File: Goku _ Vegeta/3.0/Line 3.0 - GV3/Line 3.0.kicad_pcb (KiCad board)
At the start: 2 copper layers, 206 x 197.4 mm, 111 parts, among them J1 BATTERY POWER, J10 Motor 4, J11 LEFT HEADERS, J12 RIGHT HEADERS, J13 MID HEADERS, J2 BACKUP 5V, J3 BACKUP 3V3, J4 I2C, J5 Kicker Voltmeter, J6 Solenoid, J7 Motor 1, J8 Motor 2, J9 Motor 3, Q1 BSC040N10NS5, U1 TPS62132, U2 TPS62133, U3 LM2587S-ADJ, U4 TB67H420FTG Dual/Single Motor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, U5 TB67H420FTG Dual/Single Motor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, U6 TB67H420FTG Dual/Single Motor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, U7 TB67H420FTG Dual/Single Motor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, U8 DEV-16771

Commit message: LINE PCB 3.0 BASICALLY DONE!! NOW JUST GOTTA ADD SILKSCREEN!
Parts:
- removed C1, C2: 10uF, Capacitor_SMD:C_0805_2012Metric
- removed C3, C4: 0.1uF, Capacitor_SMD:C_0805_2012Metric
- removed C5, C6: 3.3nF, Capacitor_SMD:C_0805_2012Metric
- removed C7, C8: 22uF, Capacitor_SMD:C_0805_2012Metric
- removed D1, D2: STTH2002G-TR, Package_TO_SOT_SMD:TO-263-2
- removed J5: Kicker Voltmeter, TerminalBlock:TerminalBlock_bornier-2_P5.08mm
- removed L1, L2: 2.2uH, Inductor_SMD:L_Bourns_SRR1260
- removed R33, R34: 100K, Resistor_SMD:R_0805_2012Metric
- added C14: 100uF, Capacitor_THT:CP_Radial_D10.0mm_P5.00mm, F.Cu at (116.8, 87.5)
- added LED17: JB2835AWT-W-U30GA0000-N0000001, JB2835AWT-W-U30GA0000-N0000001:LED_J2835_CRW, B.Cu at (103.0, 150.0)
- added R37: CT6EP103, POT_CT-6EP_NDC:POT_CT-6EP_NDC, F.Cu at (159.8, 141.4)
- D3: footprint Diode_SMD:D_SOD-128 -> Diode_SMD:D_SMC
- U1: value TPS62132 -> ~; footprint Package_DFN_QFN:VQFN-16-1EP_3x3mm_P0.5mm_EP1.68x1.68mm_ThermalVias -> Converter_DCDC:DC-DC Multi-output Buck Converter
- U2: value TPS62133 -> ~; footprint Package_DFN_QFN:VQFN-16-1EP_3x3mm_P0.5mm_EP1.68x1.68mm_ThermalVias -> Converter_DCDC:DC-DC Multi-output Buck Converter
- moved U2 218.4 mm to (163.3, 230.0), turned to 90 degrees
- moved U1 202.8 mm to (116.8, 230.0), turned to 90 degrees
- moved C13 178.1 mm to (175.2, 84.5), turned to 180 degrees
- moved R36 175.0 mm to (151.7, 156.1), turned to 180 degrees
- moved R35 170.6 mm to (151.7, 145.6), turned to 180 degrees
- moved C9 170.5 mm to (158.5, 162.1), turned to 180 degrees
- moved R38 163.2 mm to (148.2, 143.6)
- moved D3 161.4 mm to (144.2, 151.8), turned to -90 degrees
- moved L3 157.6 mm to (134.0, 150.0)
- moved U3 157.5 mm to (160.6, 150.9)
- moved C10 152.0 mm to (148.2, 145.6), turned to 180 degrees
- moved C11 149.9 mm to (183.2, 87.5)
- moved D4 142.0 mm to (168.0, 100.2), turned to 90 degrees
- moved C12 140.5 mm to (124.8, 84.5)
- moved J6 135.1 mm to (128.5, 101.6), turned to 90 degrees
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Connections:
- J10 pad 5: /29 -> /32
- U1 pad 1: Net-(L1-Pad1) -> GND
- U1 pad 2: Net-(L1-Pad1) -> +15V
- U1 pad 3: Net-(L1-Pad1) -> GND
- U1 pad 4: Net-(U1-PG) -> +3V3
- U2 pad 1: Net-(L2-Pad1) -> GND
- U2 pad 2: Net-(L2-Pad1) -> +15V
- U2 pad 3: Net-(L2-Pad1) -> GND
- U2 pad 4: Net-(U2-PG) -> +5V
- U6 pad 6: /32 -> /29
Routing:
- net +3V3: track 419.4 -> 754.4 mm, vias 18 -> 13
- net Net-(D3-K): track 0.00 -> 197.1 mm, vias 0 -> 3
- net +5V: track 18.2 -> 208.7 mm
- net /13: track 3.38 -> 123.3 mm, vias 0 -> 1
- net GND: track 0.00 -> 95.2 mm, vias 0 -> 19
- net Net-(D4-K): track 0.00 -> 85.7 mm
- net /15: track 7.49 -> 79.6 mm
- net Net-(U3-FB): track 0.00 -> 21.0 mm
- net Net-(D3-A): track 0.00 -> 14.3 mm
- net /29: track 112.0 -> 119.6 mm
- net Net-(R37-Pad3): track 0.00 -> 6.66 mm
- net /19: track 102.4 -> 108.4 mm
- net Net-(U7-HBMODE): track 0.00 -> 5.08 mm
- net Net-(U6-HBMODE): track 0.00 -> 5.08 mm
- net Net-(U5-HBMODE): track 0.00 -> 5.08 mm
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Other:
- outline, holes or cut-outs redrawn
- board text added: "TEENSY 4.1 3V3 LINES NOT CONNECTED"
- board text removed: "NOTE: ALL TEENSY 4.1 3V3 LINES ARE NOT CONNECTED"

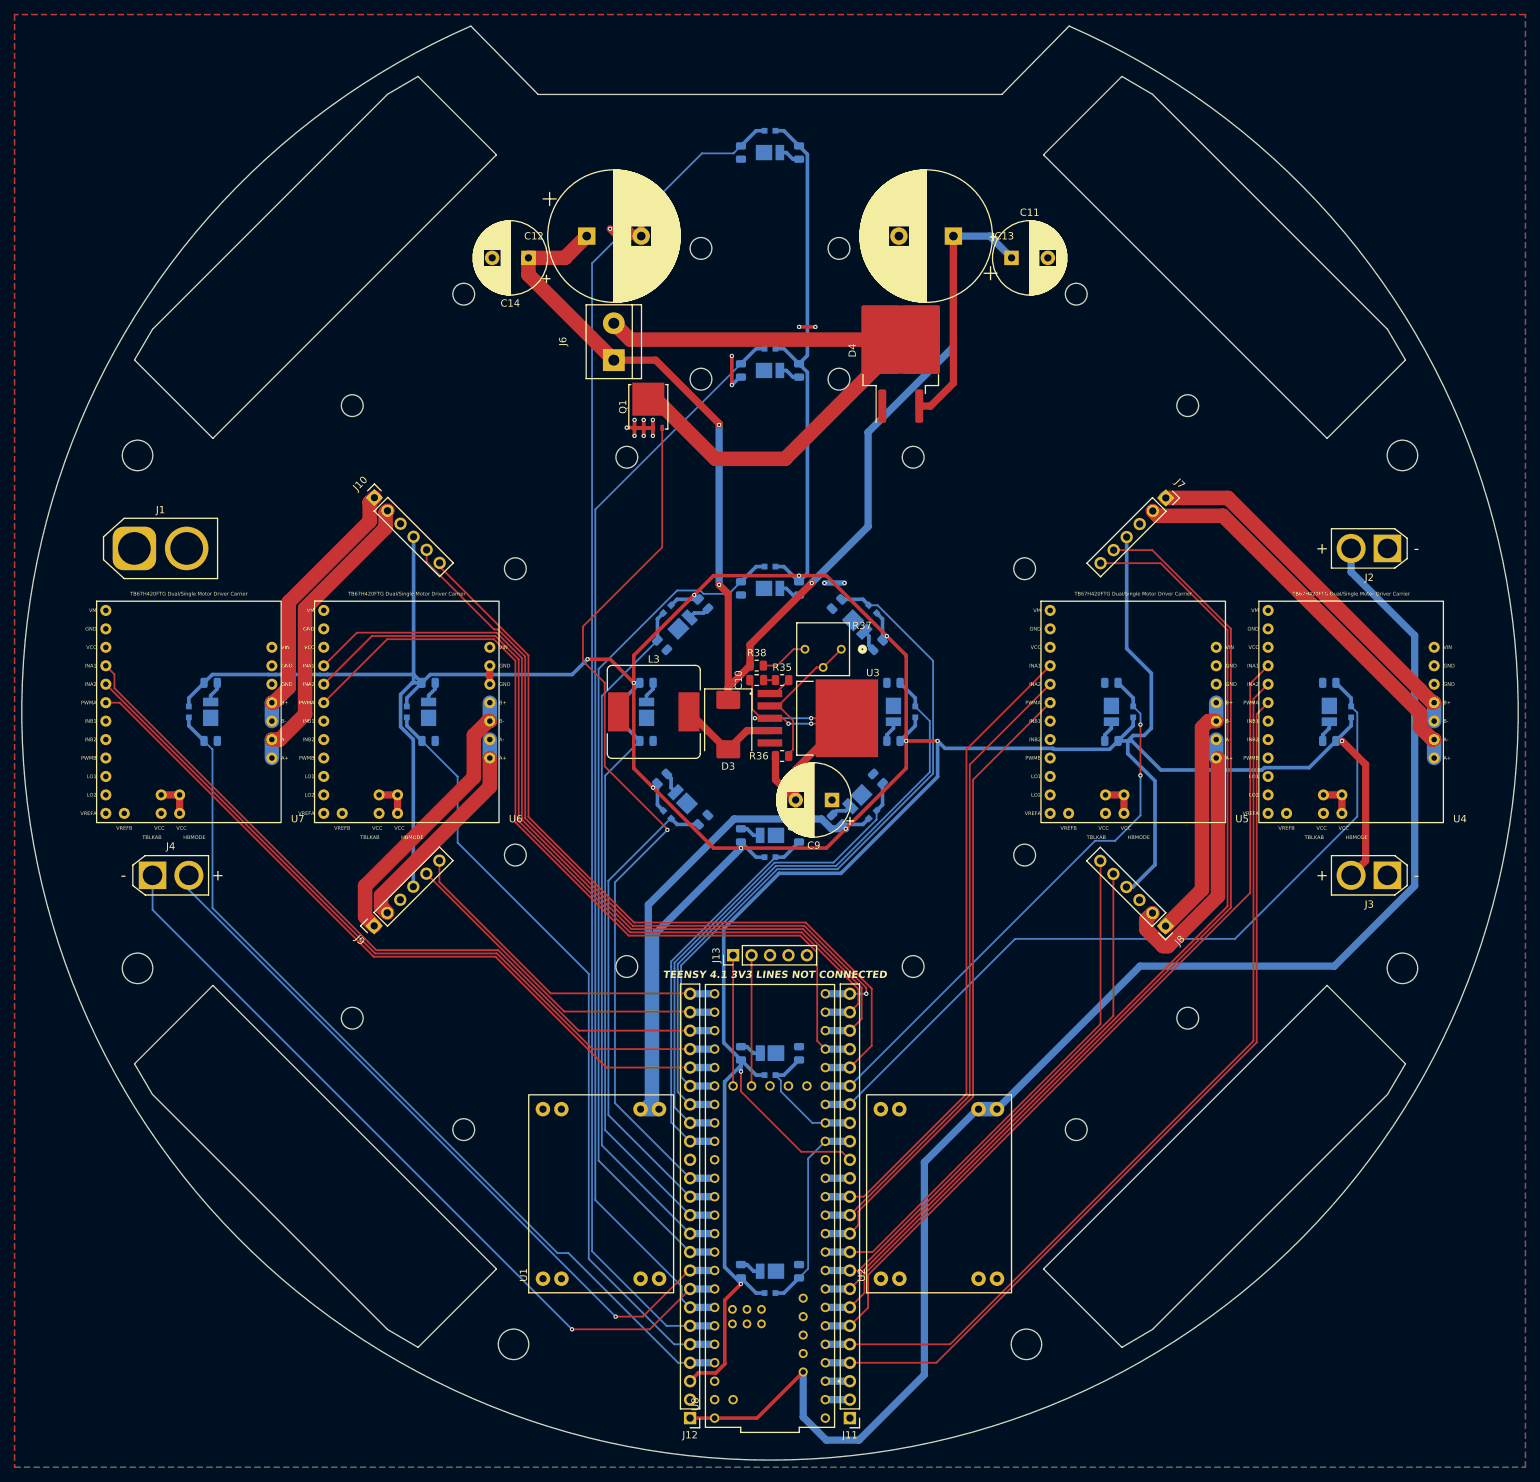
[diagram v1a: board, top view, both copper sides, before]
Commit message: LINE 3.0 Update
-Updated to have caps on power rails
-imrpoves tolerance of 100uf capacitor
-main power cable went from xt60 to xt30
- remove outer wheel guard
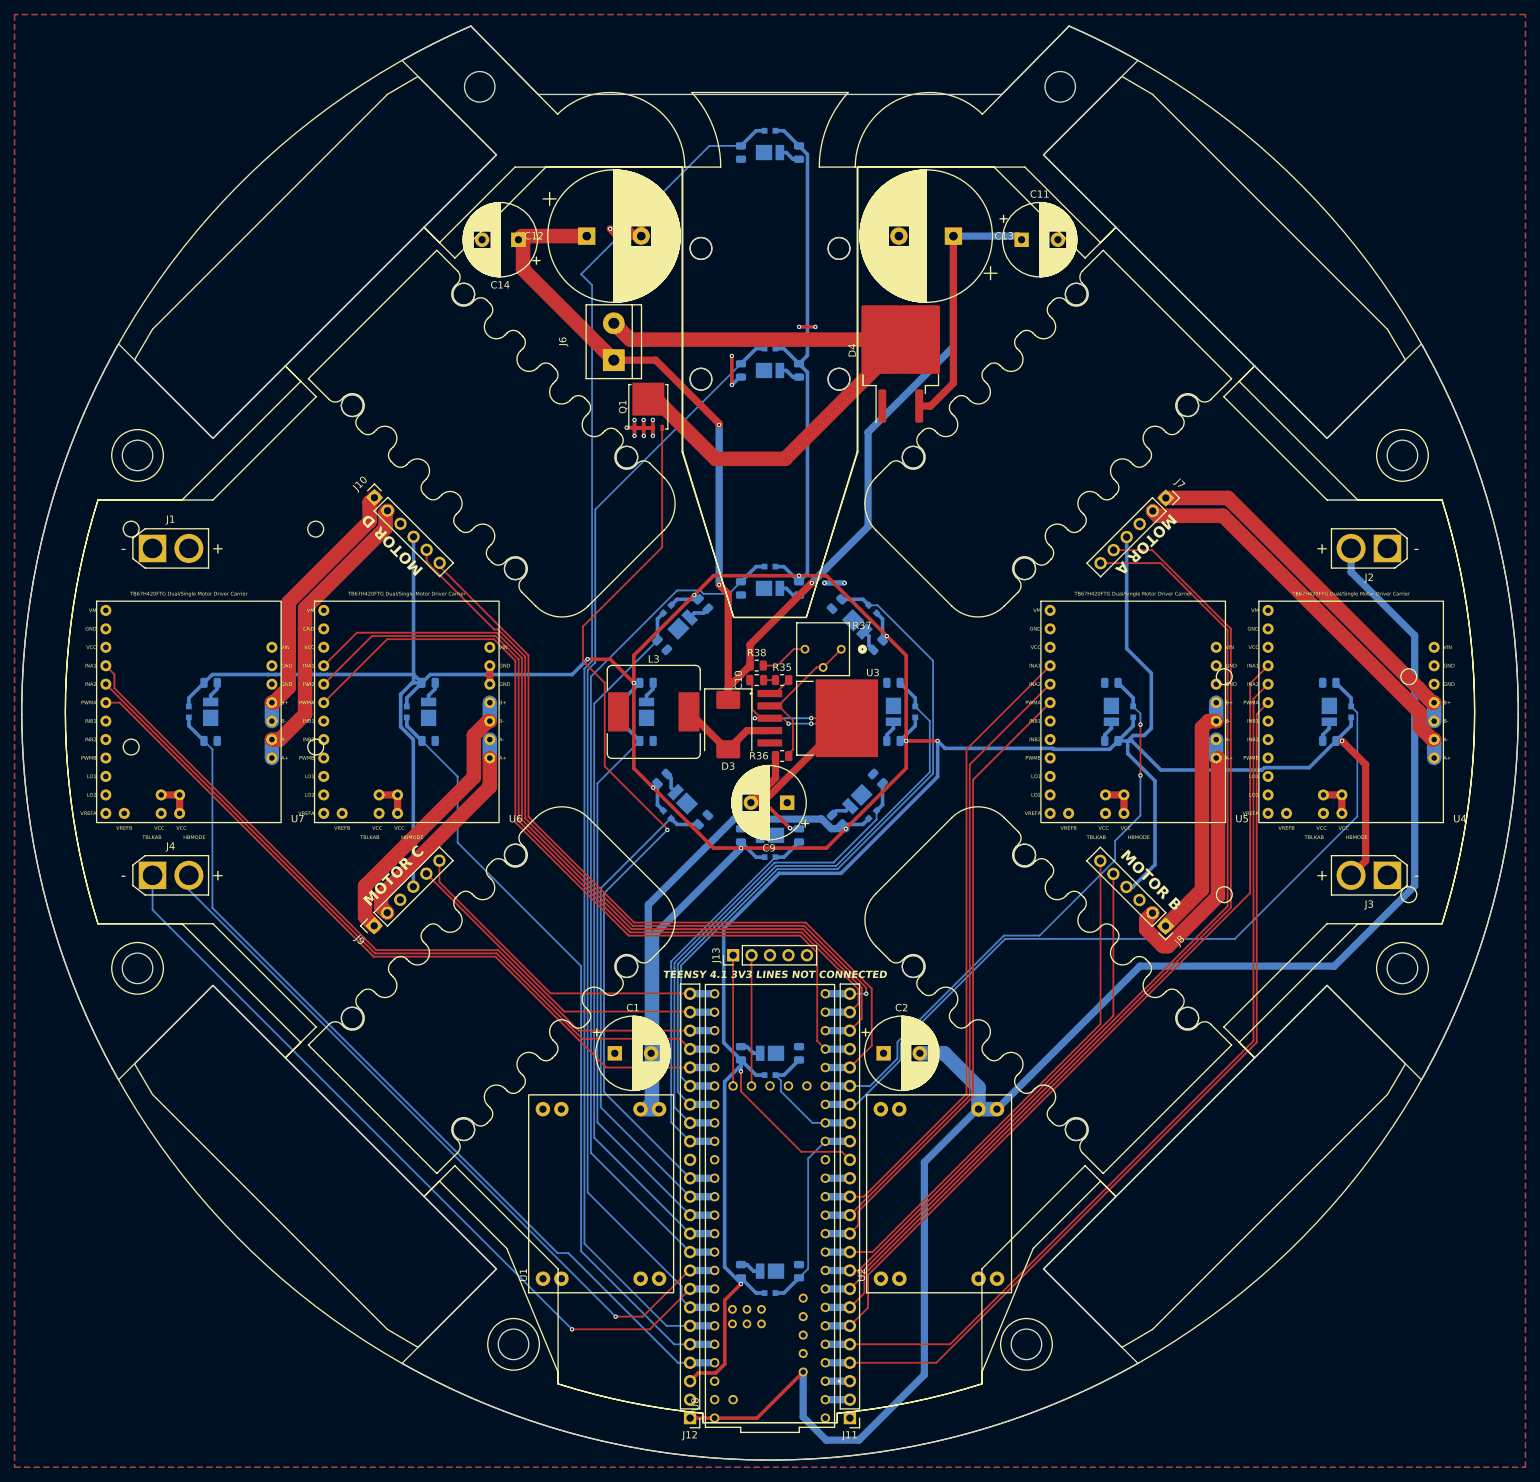
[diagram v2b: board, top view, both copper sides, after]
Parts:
- removed LED17: JB2835AWT-W-U30GA0000-N0000001, JB2835AWT-W-U30GA0000-N0000001:LED_J2835_CRW
- added C1: 100uF, Capacitor_THT:CP_Radial_D10.0mm_P5.00mm, F.Cu at (128.6, 197.0)
- added C2: 100uF, Capacitor_THT:CP_Radial_D10.0mm_P5.00mm, F.Cu at (165.6, 197.0)
- J1: footprint Connector_AMASS:AMASS_XT60-F_1x02_P7.20mm_Vertical -> Connector_AMASS:AMASS_XT30U-F_1x02_P5.0mm_Vertical
- moved LED8 66.5 mm to (103.0, 150.0), turned to 90 degrees
- moved C9 6.18 mm to (152.4, 162.5)
- moved C11 2.86 mm to (184.6, 85.0)
- moved C14 2.86 mm to (115.4, 85.0)
- moved J1 2.50 mm to (65.0, 127.5)
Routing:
- net +5V: track 208.7 -> 221.7 mm
- net GND: track 95.2 -> 103.3 mm
- net Net-(D3-K): track 197.1 -> 200.8 mm
- net /27: track 78.3 -> 81.2 mm
- net /21: track 188.4 -> 190.6 mm
- net /26: track 109.3 -> 110.6 mm
- net /13: track 123.3 -> 124.5 mm
- net /17: track 117.9 -> 118.8 mm
- net /15: track 79.6 -> 80.5 mm
- net /16: track 97.4 -> 98.2 mm
- net /20: track 151.1 -> 152.0 mm
- net /14: track 67.8 -> 68.7 mm
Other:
- outline, holes or cut-outs redrawn
- board text added: "Designed by Hugh Phan - September 2023"
- board text added: "Fort Street's Team Silverback Hugh Phan Jayden Nguyen Issey Lee Jack Sumner KZ KC"
- board text added: "MOTOR A"
- board text added: "MOTOR B"
- board text added: "MOTOR C"
- board text added: "MOTOR D"

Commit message: move to 3.1
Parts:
- moved J1 14.1 mm to (78.8, 124.5)
- moved J2 14.1 mm to (221.2, 124.5)
- moved J3 14.1 mm to (221.2, 175.5)
- moved J4 14.1 mm to (78.8, 175.5)
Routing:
- net /6: track 136.9 -> 124.3 mm
- net /19: track 108.4 -> 99.7 mm
- net /18: track 101.5 -> 92.8 mm
- net +3V3: track 754.4 -> 760.4 mm
- net +5V: track 221.7 -> 220.0 mm
- net Net-(J7-Pin_2): track 55.5 -> 54.3 mm
- net /23: track 122.7 -> 121.8 mm
- net /35: track 105.7 -> 105.2 mm
